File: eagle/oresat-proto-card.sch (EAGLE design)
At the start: 123 parts, among them J1 J-SAMTEC-TFM-110-X1-XXX-D-RA, J2 U.FL, J3 U.FL, J4 U.FL, J6 J-SAMTEC-TFM-120-X1-XXX-D-RA, J7 FTSH-105-XX-X-DV-K, Q1 DMP2240UDM, Q2 DMP2240UDM, Q3 MOSFET-PCH-SOT23-6, Q4 MOSFET-PCH-SOT23-6, Q5 PMV45EN, Q6 PMV45EN, U2 TCAN330, U3 MAX7310ATE, U4 MAX4211CETE, U5 TPS62111RSA, U6 STM32F042K6, X1 16MHZ-2.5x2mm

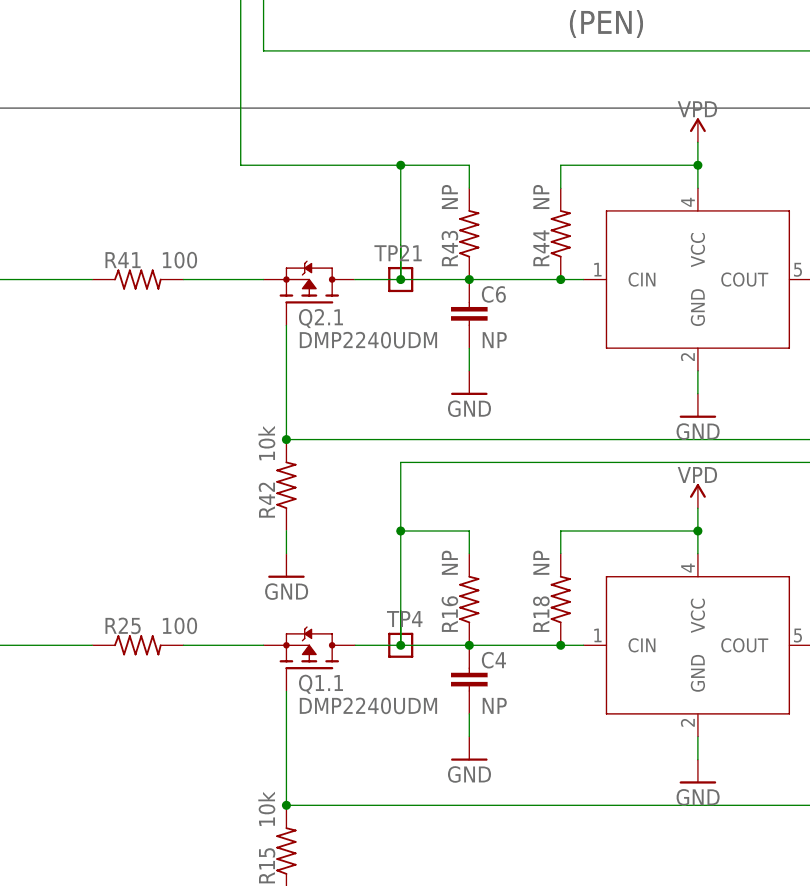
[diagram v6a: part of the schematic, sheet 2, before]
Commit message: fixed j-tag connect, final tweaks for 3.3, updated bom
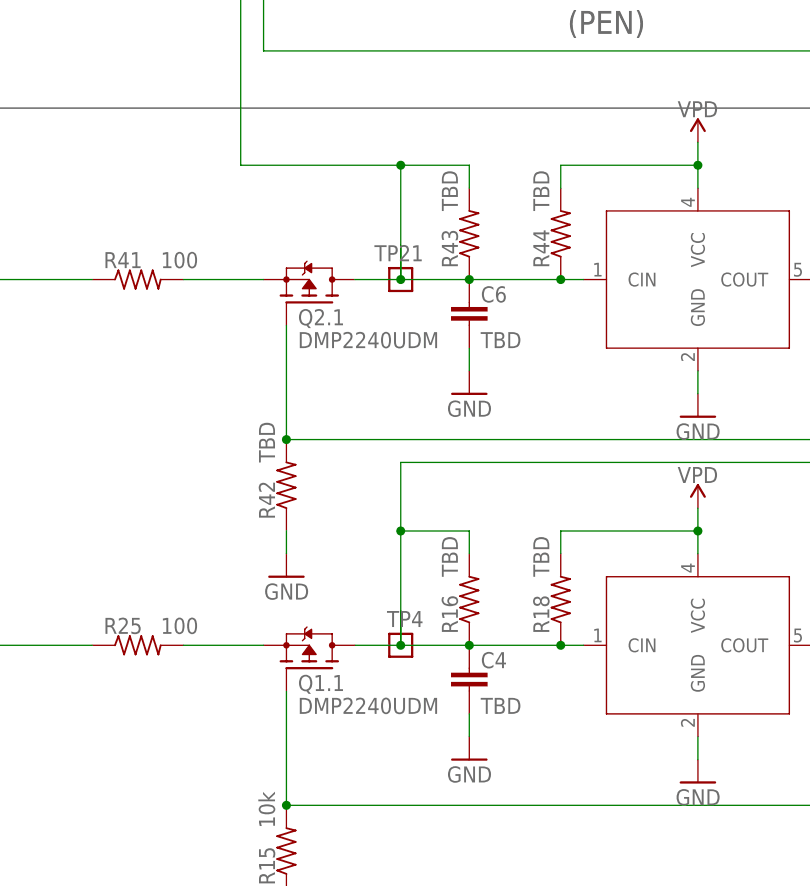
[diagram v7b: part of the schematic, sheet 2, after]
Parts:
- C4, C6, R16, R18, R43, R44: value NP -> TBD
- R42: value 10k -> TBD
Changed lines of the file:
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@@
 <layer number="115" name="ReferenceISLANDS" color="7" fill="1" visible="no" active="yes"/>
 <layer number="116" name="Patch_BOT" color="7" fill="1" visible="yes" active="yes"/>
+<layer number="117" name="BACKMAAT1" color="7" fill="1" visible="yes" active="yes"/>
 <layer number="118" name="Rect_Pads" color="7" fill="1" visible="no" active="yes"/>
+<layer number="119" name="KAP_TEKEN" color="7" fill="1" visible="yes" active="yes"/>
+<layer number="120" name="KAP_MAAT1" color="7" fill="1" visible="yes" active="yes"/>
 <layer number="121" name="_tsilk" color="7" fill="1" visible="yes" active="yes"/>
 <layer number="122" name="_bsilk" color="7" fill="1" visible="yes" active="yes"/>
@@
 <layer number="128" name="_bValues" color="7" fill="1" visible="yes" active="yes"/>
 <layer number="129" name="Mask" color="7" fill="1" visible="yes" active="yes"/>
+<layer number="130" name="SMDSTROOK" color="7" fill="1" visible="yes" active="yes"/>
 <layer number="131" name="tAdjust" color="7" fill="1" visible="yes" active="yes"/>
 <layer number="132" name="bAdjust" color="7" fill="1" visible="yes" active="yes"/>
+<layer number="133" name="bottom_silk" color="7" fill="1" visible="yes" active="yes"/>
+<layer number="134" name="silk_top" color="7" fill="1" visible="yes" active="yes"/>
+<layer number="135" name="silk_bottom" color="7" fill="1" visible="yes" active="yes"/>
+<layer number="136" name="silktop" color="7" fill="1" visible="yes" active="yes"/>
+<layer number="137" name="silkbottom" color="7" fill="1" visible="yes" active="yes"/>
+<layer number="140" name="Testjig_Mill" color="26" fill="1" visible="yes" active="yes"/>
 <layer number="144" name="Drill_legend" color="7" fill="1" visible="yes" active="yes"/>
+<layer number="145" name="DrillLegend_01-16" color="7" fill="1" visible="yes" active="yes"/>
+<layer number="146" name="DrillLegend_01-20" color="7" fill="1" visible="yes" active="yes"/>
 <layer number="150" name="Notes" color="7" fill="1" visible="yes" active="yes"/>
 <layer number="151" name="HeatSink" color="7" fill="1" visible="yes" active="yes"/>
@@
 <layer number="230" name="230bmp" color="7" fill="1" visible="yes" active="yes"/>
 <layer number="231" name="231bmp" color="7" fill="1" visible="yes" active="yes"/>
+<layer number="232" name="Eagle3D_PG2" color="7" fill="1" visible="no" active="no"/>
+<layer number="233" name="Eagle3D_PG3" color="7" fill="1" visible="no" active="no"/>
 <layer number="248" name="Housing" color="7" fill="1" visible="yes" active="yes"/>
 <layer number="249" name="Edge" color="7" fill="1" visible="yes" active="yes"/>
@@
 <part name="TP3" library="Tova" deviceset="TEST-POINT" device=""/>
 <part name="TP5" library="Tova" deviceset="TEST-POINT" device=""/>
-<part name="R16" library="rcl_custom" deviceset="R-US_" device="0402-B-NOSILK" value="NP">
-<attribute name="DIS" value="Digi-Key"/>
-<attribute name="DPN" value="1276-4275-1-ND"/>
-<attribute name="MFR" value="Samsung"/>
-<attribute name="MPN" value="RC1005F6653CS"/>
-</part>
-<part name="R18" library="rcl_custom" deviceset="R-US_" device="0402-B-NOSILK" value="NP">
+<part name="R16" library="rcl_custom" deviceset="R-US_" device="0402-B-NOSILK" value="TBD">
+<attribute name="DIS" value="Digi-Key"/>
+<attribute name="DPN" value="1276-4275-1-ND"/>
+<attribute name="MFR" value="Samsung"/>
+<attribute name="MPN" value="RC1005F6653CS"/>
+</part>
+<part name="R18" library="rcl_custom" deviceset="R-US_" device="0402-B-NOSILK" value="TBD">
 <attribute name="DIS" value="Digi-Key"/>
 <attribute name="DPN" value="1276-4275-1-ND"/>
@@
 <part name="GND44" library="supply1" library_urn="urn:adsk.eagle:library:371" deviceset="GND" device=""/>
 <part name="VPD4" library="oresat-supplies" deviceset="VPD" device=""/>
-<part name="C4" library="oresat-rcl" deviceset="C-EU" device="0805-B-NOSILK" value="NP"/>
+<part name="C4" library="oresat-rcl" deviceset="C-EU" device="0805-B-NOSILK" value="TBD"/>
 <part name="GND45" library="supply1" library_urn="urn:adsk.eagle:library:371" deviceset="GND" device=""/>
 <part name="TP4" library="Tova" deviceset="TEST-POINT" device=""/>
@@
 <attribute name="MPN" value="DMP2240UDM"/>
 </part>
-<part name="R42" library="rcl_custom" deviceset="R-US_" device="0402-B-NOSILK" value="10k">
+<part name="R42" library="rcl_custom" deviceset="R-US_" device="0402-B-NOSILK" value="TBD">
 <attribute name="DIS" value="Digi-Key"/>
 <attribute name="DPN" value="1276-4275-1-ND"/>
@@
 </part>
 <part name="GND49" library="supply1" library_urn="urn:adsk.eagle:library:371" deviceset="GND" device=""/>
-<part name="R43" library="rcl_custom" deviceset="R-US_" device="0402-B-NOSILK" value="NP">
-<attribute name="DIS" value="Digi-Key"/>
-<attribute name="DPN" value="1276-4275-1-ND"/>
-<attribute name="MFR" value="Samsung"/>
-<attribute name="MPN" value="RC1005F6653CS"/>
-</part>
-<part name="R44" library="rcl_custom" deviceset="R-US_" device="0402-B-NOSILK" value="NP">
+<part name="R43" library="rcl_custom" deviceset="R-US_" device="0402-B-NOSILK" value="TBD">
+<attribute name="DIS" value="Digi-Key"/>
+<attribute name="DPN" value="1276-4275-1-ND"/>
+<attribute name="MFR" value="Samsung"/>
+<attribute name="MPN" value="RC1005F6653CS"/>
+</part>
+<part name="R44" library="rcl_custom" deviceset="R-US_" device="0402-B-NOSILK" value="TBD">
 <attribute name="DIS" value="Digi-Key"/>
 <attribute name="DPN" value="1276-4275-1-ND"/>
@@
 <part name="GND50" library="supply1" library_urn="urn:adsk.eagle:library:371" deviceset="GND" device=""/>
 <part name="VPD5" library="oresat-supplies" deviceset="VPD" device=""/>
-<part name="C6" library="oresat-rcl" deviceset="C-EU" device="0805-B-NOSILK" value="NP"/>
+<part name="C6" library="oresat-rcl" deviceset="C-EU" device="0805-B-NOSILK" value="TBD"/>
 <part name="GND51" library="supply1" library_urn="urn:adsk.eagle:library:371" deviceset="GND" device=""/>
 <part name="TP21" library="Tova" deviceset="TEST-POINT" device=""/>

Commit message: Now v3.3. New OPD I2C protection circuits. Move to 4 layers. Lots of cleanup and massaging, but nothing worth saying. Added ground ring around 3.3V ring on L15. Attributes are still wrong, needs to be cleaned up to make automatic BOM.
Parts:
- removed Q2: DMP2240UDM, Q-MOSFET-PCH-dual-SOT23-6:MOSFET-PCH-SOT23-6
- removed TP21, TP4: TEST-POINT, Tova:TEST-POINT
- removed U$2, U$3: MIC842, Q-Microchip-MIC842-Comparator:MIC842
- added U1, U7: MIC842LYC5, Q-Microchip-MIC842-Comparator:MIC842
- C4, C6: value TBD -> 1u; device oresat-rcl:C-EU0805-B-NOSILK -> oresat-rcl:C-EU0603-B-NOSILK; DIS (none) -> Digi-Key; DPN (none) -> 1276-1001-1-ND; MFR (none) -> Samsung; MPN (none) -> CL05B104KO5NNNC
- R16, R43: value TBD -> 330k
- R18, R44: value TBD -> 1M
- R42: value TBD -> 10k
- U4: value MAX4211CETE -> MAX4211FETE; MPN MAX4211CETE -> MAX4211FETE
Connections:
- new net N$400: C6.1, R43.1, R44.1, U1.CIN
- new net N$401: C4.1, R16.1, R18.1, U7.CIN
- new net PA15: JP4.11, U6.PA15
- net GND: now also U1.GND, U7.GND; no longer U$2.GND, U$3.GND
- net IOUT: no longer JP4.11, U6.PA15
- net N$479: now also Q1.2.S; no longer Q2.1.S
- net N$480: now also Q1.2.G, U1.COUT; no longer Q2.1.G, U$3.COUT
- net N$580: now also U7.COUT; no longer U$2.COUT
- net PEN-SCL-FILT: now also Q1.2.D; no longer C6.1, Q2.1.D, R43.1, R44.1, TP21.1, U$3.CIN
- net PEN-SDA-FILT: no longer C4.1, R16.1, R18.1, TP4.1, U$2.CIN
- net VPD: now also U1.VCC, U7.VCC; no longer U$2.VCC, U$3.VCC
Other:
- note added: "To STM32 I2C bootloader"
- note removed: "OreSat Power Enable (PEN)"
- moved on the sheet: C1, C2, C4, C5, C6, D1, D4, Q1.1, Q3, Q4, Q5, Q6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
